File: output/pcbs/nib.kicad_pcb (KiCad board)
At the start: 2 copper layers, 152.8 x 120 mm, 65 parts

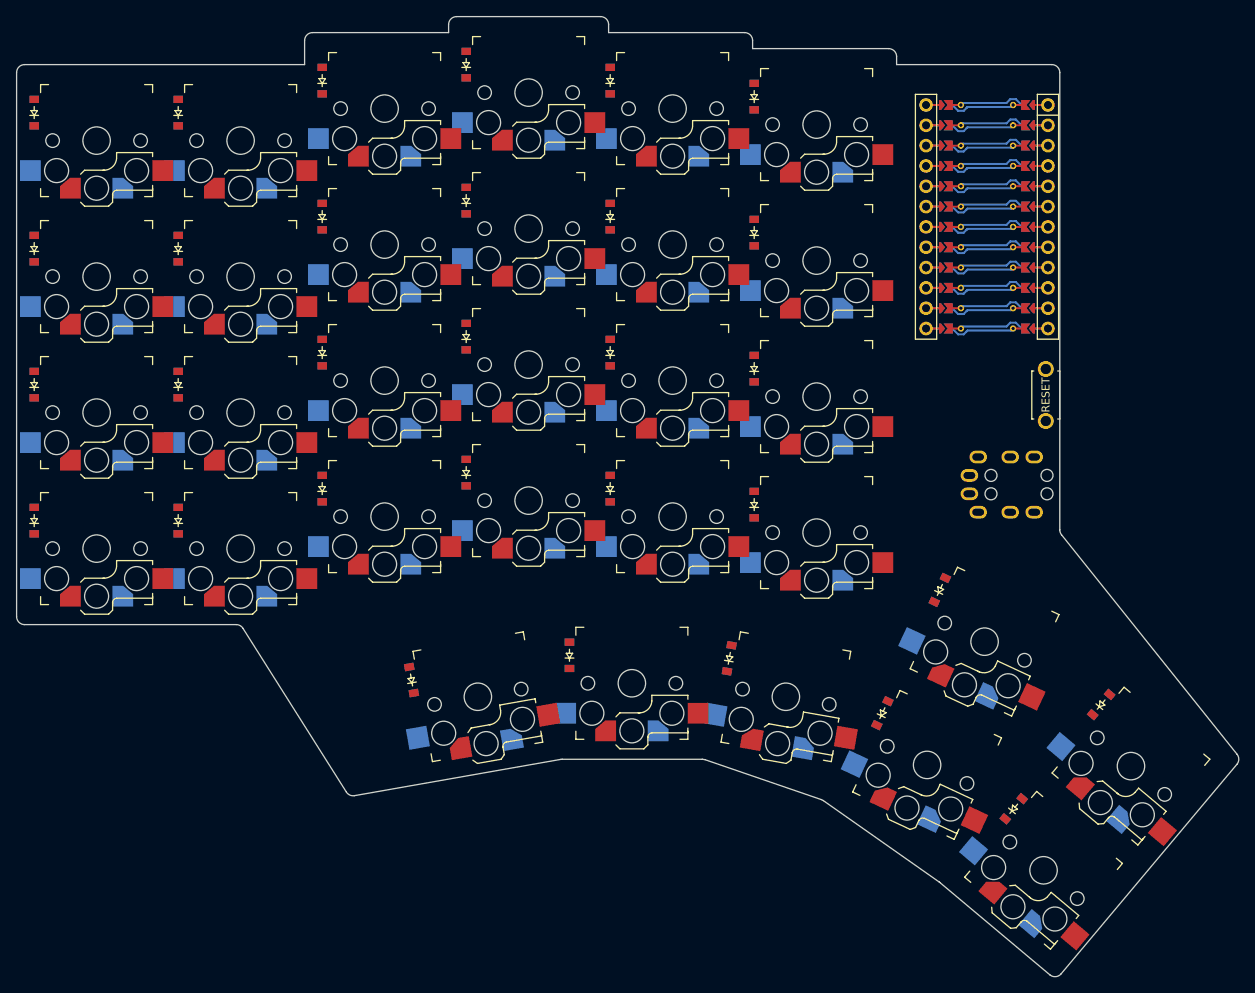
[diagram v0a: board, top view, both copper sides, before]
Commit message: edit footprints
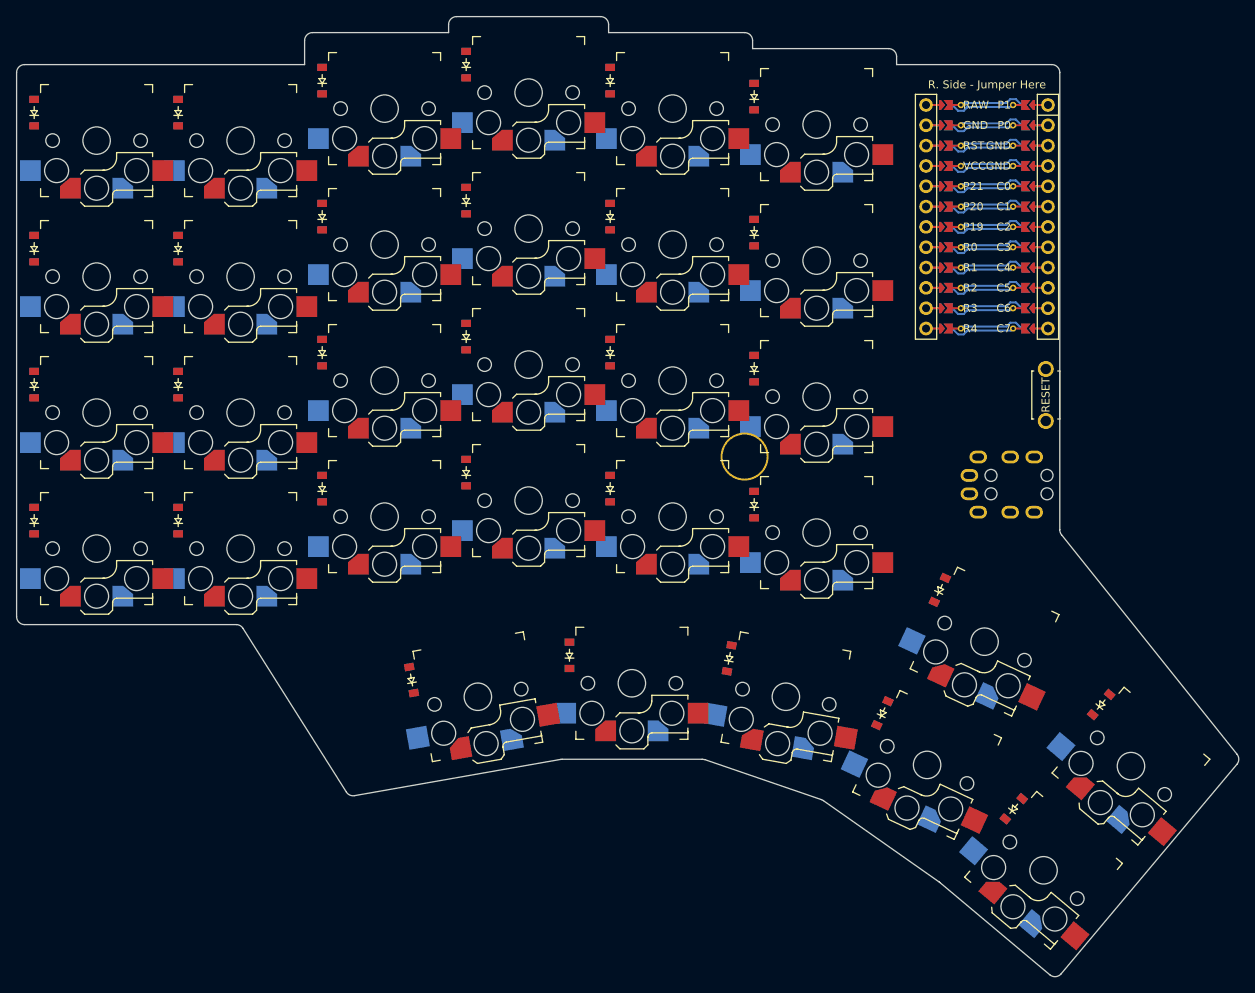
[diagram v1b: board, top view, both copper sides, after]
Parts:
- added TP1: , trackpoint_mount_t430, F.Cu at (181.0, 88.5)
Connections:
- MCU1 pad 113: R4 -> C7
- MCU1 pad 114: R3 -> C6
- MCU1 pad 115: R2 -> C5
- MCU1 pad 116: R1 -> C4
- MCU1 pad 117: R0 -> C3
- MCU1 pad 118: P19 -> C2
- MCU1 pad 119: P20 -> C1
- MCU1 pad 120: P21 -> C0
- MCU1 pad 121: VCC -> GND
- MCU1 pad 122: RST -> GND
- MCU1 pad 123: GND -> P0
- MCU1 pad 124: RAW -> P1

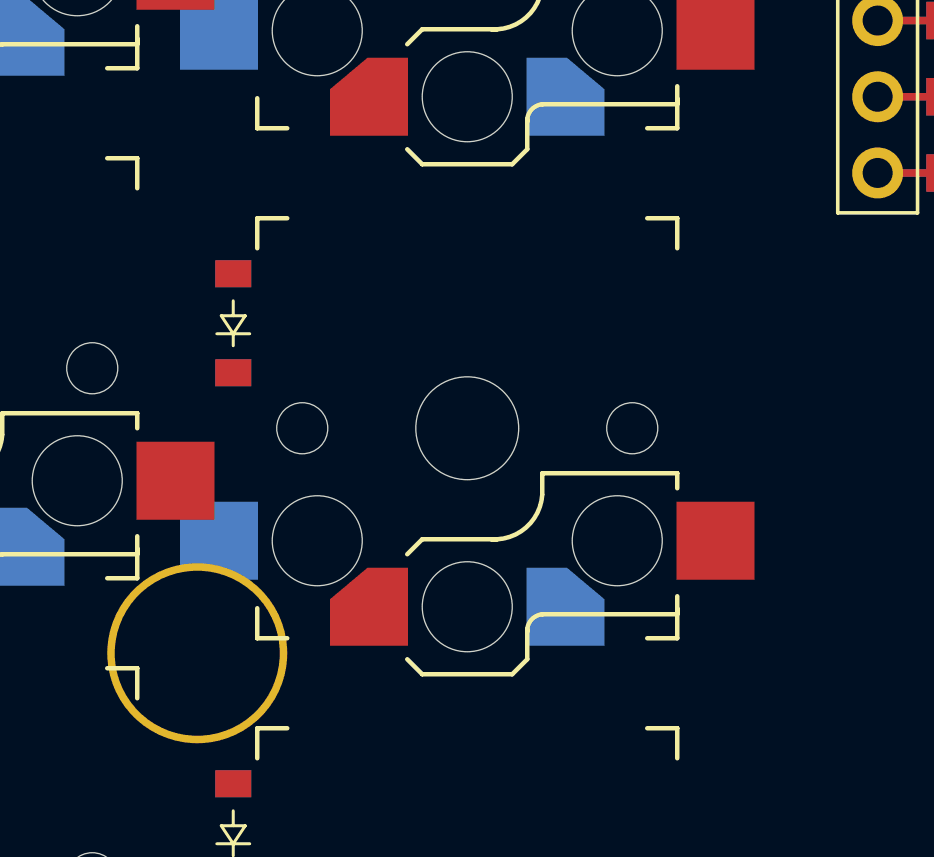
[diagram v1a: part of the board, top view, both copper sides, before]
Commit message: edit footprint. rotate matrix_inner_home
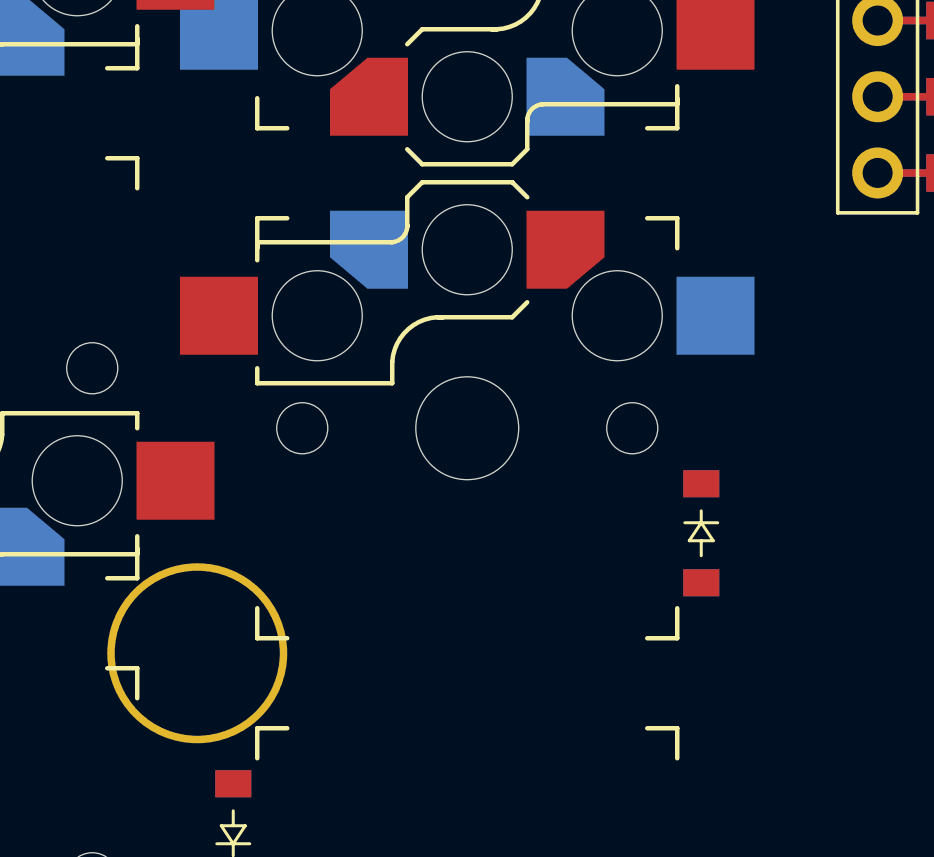
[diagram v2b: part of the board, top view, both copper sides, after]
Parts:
- moved D22 17.1 mm to (197.8, 84.5), turned to 270 degrees
- turned S22 to 360 degrees
- turned TP1 to 45 degrees
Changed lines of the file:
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@@
         )
             (module PG1350 (layer F.Cu)
-            (at 190 81 180)
+            (at 190 81 360)
             (attr virtual)
             (fp_text reference "S22" (at 0 0) (layer F.SilkS) hide (effects (font (size 1.27 1.27) (thickness 0.15))))
@@
             (fp_arc (start 2.499999 -6.7) (end 2 -6.690001) (angle -88.9) (layer B.SilkS) (width 0.15))
             (fp_arc (start 0.97 -2.17) (end 2.5 -2.17) (angle -90) (layer B.SilkS) (width 0.15))
-            (pad 1 smd custom (at -3.275 -5.95 180) (size 1 1) (layers B.Cu B.Paste B.Mask)
+            (pad 1 smd custom (at -3.275 -5.95 360) (size 1 1) (layers B.Cu B.Paste B.Mask)
                 (zone_connect 0)
                 (options (clearance outline) (anchor rect))
@@
                 ) (width 0))
             ) (net 20 "C5"))
-            (pad 2 smd rect (at 8.275 -3.75 180) (size 2.6 2.6) (layers B.Cu B.Paste B.Mask) (net 68 "inner_home"))
+            (pad 2 smd rect (at 8.275 -3.75 360) (size 2.6 2.6) (layers B.Cu B.Paste B.Mask) (net 68 "inner_home"))
             (pad "" np_thru_hole circle (at 5 -3.75 195) (size 3 3) (drill 3) (layers *.Cu *.Mask))
             (fp_line (start 2 -4.2) (end 1.5 -3.7) (layer F.SilkS) (width 0.15))
@@
             (fp_arc (start -0.91 -2.11) (end -0.8 -3.7) (angle -90) (layer F.SilkS) (width 0.15))
             (fp_arc (start -2.55 -6.75) (end -2.52 -6.2) (angle -90) (layer F.SilkS) (width 0.15))
-            (pad 1 connect custom (at 3.275 -5.95 180) (size 0.5 0.5) (layers F.Cu F.Mask)
+            (pad 1 connect custom (at 3.275 -5.95 360) (size 0.5 0.5) (layers F.Cu F.Mask)
                 (zone_connect 0)
                 (options (clearance outline) (anchor rect))
@@
                 ) (width 0))
             ) (net 20 "C5"))
-            (pad 2 smd rect (at -8.275 -3.75 180) (size 2.6 2.6) (layers F.Cu F.Paste F.Mask) (net 68 "inner_home"))
+            (pad 2 smd rect (at -8.275 -3.75 360) (size 2.6 2.6) (layers F.Cu F.Paste F.Mask) (net 68 "inner_home"))
             (pad "" np_thru_hole circle (at -5 -3.75 195) (size 3 3) (drill 3) (layers *.Cu *.Mask))
         )
@@
     )
     (module ComboDiode (layer F.Cu)
-        (at 182.2 77.5 90)
+        (at 197.8 84.5 270)
         (attr virtual)
         (fp_text reference "D22" (at 0 0) (layer F.SilkS) hide (effects (font (size 1.27 1.27) (thickness 0.15))))
@@
         (fp_line (start -0.35 0) (end -0.35 -0.55) (layer B.SilkS) (width 0.1))
         (fp_line (start -0.75 0) (end -0.35 0) (layer B.SilkS) (width 0.1))
-        (pad 1 smd rect (at -1.65 0 90) (size 0.9 1.2) (layers F.Cu F.Paste F.Mask) (net 10 "R2"))
-        (pad 2 smd rect (at 1.65 0 90) (size 0.9 1.2) (layers B.Cu B.Paste B.Mask) (net 68 "inner_home"))
-        (pad 1 smd rect (at -1.65 0 90) (size 0.9 1.2) (layers B.Cu B.Paste B.Mask) (net 10 "R2"))
-        (pad 2 smd rect (at 1.65 0 90) (size 0.9 1.2) (layers F.Cu F.Paste F.Mask) (net 68 "inner_home"))
+        (pad 1 smd rect (at -1.65 0 270) (size 0.9 1.2) (layers F.Cu F.Paste F.Mask) (net 10 "R2"))
+        (pad 2 smd rect (at 1.65 0 270) (size 0.9 1.2) (layers B.Cu B.Paste B.Mask) (net 68 "inner_home"))
+        (pad 1 smd rect (at -1.65 0 270) (size 0.9 1.2) (layers B.Cu B.Paste B.Mask) (net 10 "R2"))
+        (pad 2 smd rect (at 1.65 0 270) (size 0.9 1.2) (layers F.Cu F.Paste F.Mask) (net 68 "inner_home"))
     )
     (module ComboDiode (layer F.Cu)
@@
       )
       (module trackpoint_mount_t430 (layer F.Cu)
-        (at 181 88.5 0)
+        (at 181 88.5 45)
         (attr virtual)
         (fp_text reference "TP1" (at 0 0) (layer B.SilkS) hide
           (effects (font (size 1 1) (thickness 0.15)))
         )
-        (fp_circle (center 0 0) (end -3.95 0) (layer F.CrtYd) (width 0.05))
-        (fp_circle (center 0 0) (end -3.7 0) (layer Cmts.User) (width 0.15))
-        (fp_text user %R (at 0 0 180) (layer F.Fab)
-          (effects (font (size 1 1) (thickness 0.15)))
-        )
-        (fp_line (start 2.75 6.5) (end 6.25 3) (layer F.Fab) (width 0.2))
-        (fp_line (start 2.75 11.5) (end -2.75 11.5) (layer F.Fab) (width 0.2))
-        (fp_line (start -6.25 3) (end -6.25 -3) (layer F.Fab) (width 0.2))
-        (fp_line (start 6.25 3) (end 6.25 -3) (layer F.Fab) (width 0.2))
-        (fp_line (start 2.75 -11.5) (end -2.75 -11.5) (layer F.Fab) (width 0.2))
-        (fp_line (start 2.75 6.5) (end 2.75 11.5) (layer F.Fab) (width 0.2))
-        (fp_line (start -2.75 6.5) (end -2.75 11.5) (layer F.Fab) (width 0.2))
-        (fp_line (start -2.75 -11.5) (end -2.75 -6.5) (layer F.Fab) (width 0.2))
-        (fp_line (start 2.75 -11.5) (end 2.75 -6.5) (layer F.Fab) (width 0.2))
-        (fp_line (start -2.75 6.5) (end -6.25 3) (layer F.Fab) (width 0.2))
-        (fp_line (start 6.25 -3) (end 2.75 -6.5) (layer F.Fab) (width 0.2))
-        (fp_line (start -6.25 -3) (end -2.75 -6.5) (layer F.Fab) (width 0.2))
-        (fp_circle (center 0 0) (end -3.95 0) (layer B.CrtYd) (width 0.05))
-        (fp_circle (center 0 0) (end -3.7 0) (layer Cmts.User) (width 0.15))
-        (fp_line (start -6.25 -3) (end -2.75 -6.5) (layer B.Fab) (width 0.2))
-        (fp_line (start 6.25 -3) (end 2.75 -6.5) (layer B.Fab) (width 0.2))
-        (fp_line (start 2.75 6.5) (end 6.25 3) (layer B.Fab) (width 0.2))
-        (fp_line (start -2.75 6.5) (end -6.25 3) (layer B.Fab) (width 0.2))
-        (fp_line (start 6.25 3) (end 6.25 -3) (layer B.Fab) (width 0.2))
-        (fp_line (start 2.75 11.5) (end -2.75 11.5) (layer B.Fab) (width 0.2))
-        (fp_line (start -6.25 3) (end -6.25 -3) (layer B.Fab) (width 0.2))
-        (fp_line (start 2.75 -11.5) (end -2.75 -11.5) (layer B.Fab) (width 0.2))
-        (fp_line (start -2.75 6.5) (end -2.75 11.5) (layer B.Fab) (width 0.2))
-        (fp_line (start 2.75 6.5) (end 2.75 11.5) (layer B.Fab) (width 0.2))
-        (fp_line (start -2.75 -11.5) (end -2.75 -6.5) (layer B.Fab) (width 0.2))
-        (fp_line (start 2.75 -11.5) (end 2.75 -6.5) (layer B.Fab) (width 0.2))
-        (fp_line (start 38.25 12.25) (end 22.25 12.25) (layer Dwgs.User) (width 0.2))
-        (fp_line (start 22.25 2.75) (end 22.25 12.25) (layer Dwgs.User) (width 0.2))
-        (fp_line (start 22.25 -2.75) (end 22.25 2.75) (layer Dwgs.User) (width 0.2))
-        (fp_line (start 22.25 2.75) (end 6.25 2.75) (layer Dwgs.User) (width 0.2))
-        (fp_line (start 22.25 -2.75) (end 6.25 -2.75) (layer Dwgs.User) (width 0.2))
-        (fp_line (start 38.25 -22.25) (end 38.25 12.25) (layer Dwgs.User) (width 0.2))
-        (fp_line (start 38.25 -22.25) (end 22.25 -22.25) (layer Dwgs.User) (width 0.2))
-        (fp_line (start 22.25 -22.25) (end 22.25 -2.75) (layer Dwgs.User) (width 0.2))
-        (fp_line (start 6.25 -2.75) (end 6.25 2.75) (layer Dwgs.User) (width 0.2))
         (pad 1 np_thru_hole circle (at 0 0 180) (size 6 6) (drill 5.5) (layers *.Cu *.Mask))
       )

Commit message: edit mcu footprint, udpate mcu pins in config.yaml. update readme
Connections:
- net P0 renamed D1
- net P1 renamed D0

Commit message: lots of changes
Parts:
- added DISP1: HRS_FH34SRJ-8S-0.5SH_50_, HRS_FH34SRJ-8S-0.5SH_50_, F.Cu at (208.8, 90.0)
- added H1: , Screw_Hole, F.Cu at (109.0, 41.4)
- added H2: , Screw_Hole, F.Cu at (121.6, 111.0)
- added H3: , Screw_Hole, F.Cu at (200.3, 41.4)
- added H4: , Screw_Hole, F.Cu at (226.6, 109.1)
- added SW1: , power_switch, F.Cu at (218.8, 90.0)
- TRRS1: footprint TRRS-PJ-320A-dual -> ceoloide:TRRS-PJ-320A-dual (reversible, symmetric)
- moved TRRS1 53.9 mm to (226.6, 39.6), turned to 0 degrees
- moved D28 1.50 mm to (197.6, 121.9)
- moved D29 1.50 mm to (204.8, 106.5)
- moved D30 1.50 mm to (213.7, 133.7)
- moved D31 1.50 mm to (224.6, 120.6)
- moved D1 1.50 mm to (92.2, 98.0)
- moved D10 1.50 mm to (128.2, 77.0)
- moved D11 1.50 mm to (128.2, 60.0)
- moved D12 1.50 mm to (128.2, 43.0)
- moved D13 1.50 mm to (146.2, 92.0)
- moved D14 1.50 mm to (146.2, 75.0)
- moved D15 1.50 mm to (146.2, 58.0)
- moved D16 1.50 mm to (146.2, 41.0)
- moved D17 1.50 mm to (164.2, 94.0)
- moved D18 1.50 mm to (164.2, 77.0)
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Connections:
- MCU1 pad 124: D0 -> SP
- TRRS1 pad 1: data -> SP
- TRRS1 pad 2: data -> GND
- TRRS1 pad 3: GND -> VCC
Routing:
- net SP: track 0.00 -> 121.9 mm
- net D0: track 121.9 -> 0.00 mm
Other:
- outline, holes or cut-outs redrawn
